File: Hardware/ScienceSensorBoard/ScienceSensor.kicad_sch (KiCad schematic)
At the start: 75 parts, among them U2 OKI-78SR-3.3_1.5-W36H-C

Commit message: Updated BOM and annotation
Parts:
- removed C2: CP1, symbol ScienceSensor-rescue:CP1-Device
- added C2: 10 uF, symbol Device:C_Polarized_US
- gave numbers to parts that had none: 63
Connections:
- net +12V: now also C2.1
- net GND: now also C2.2

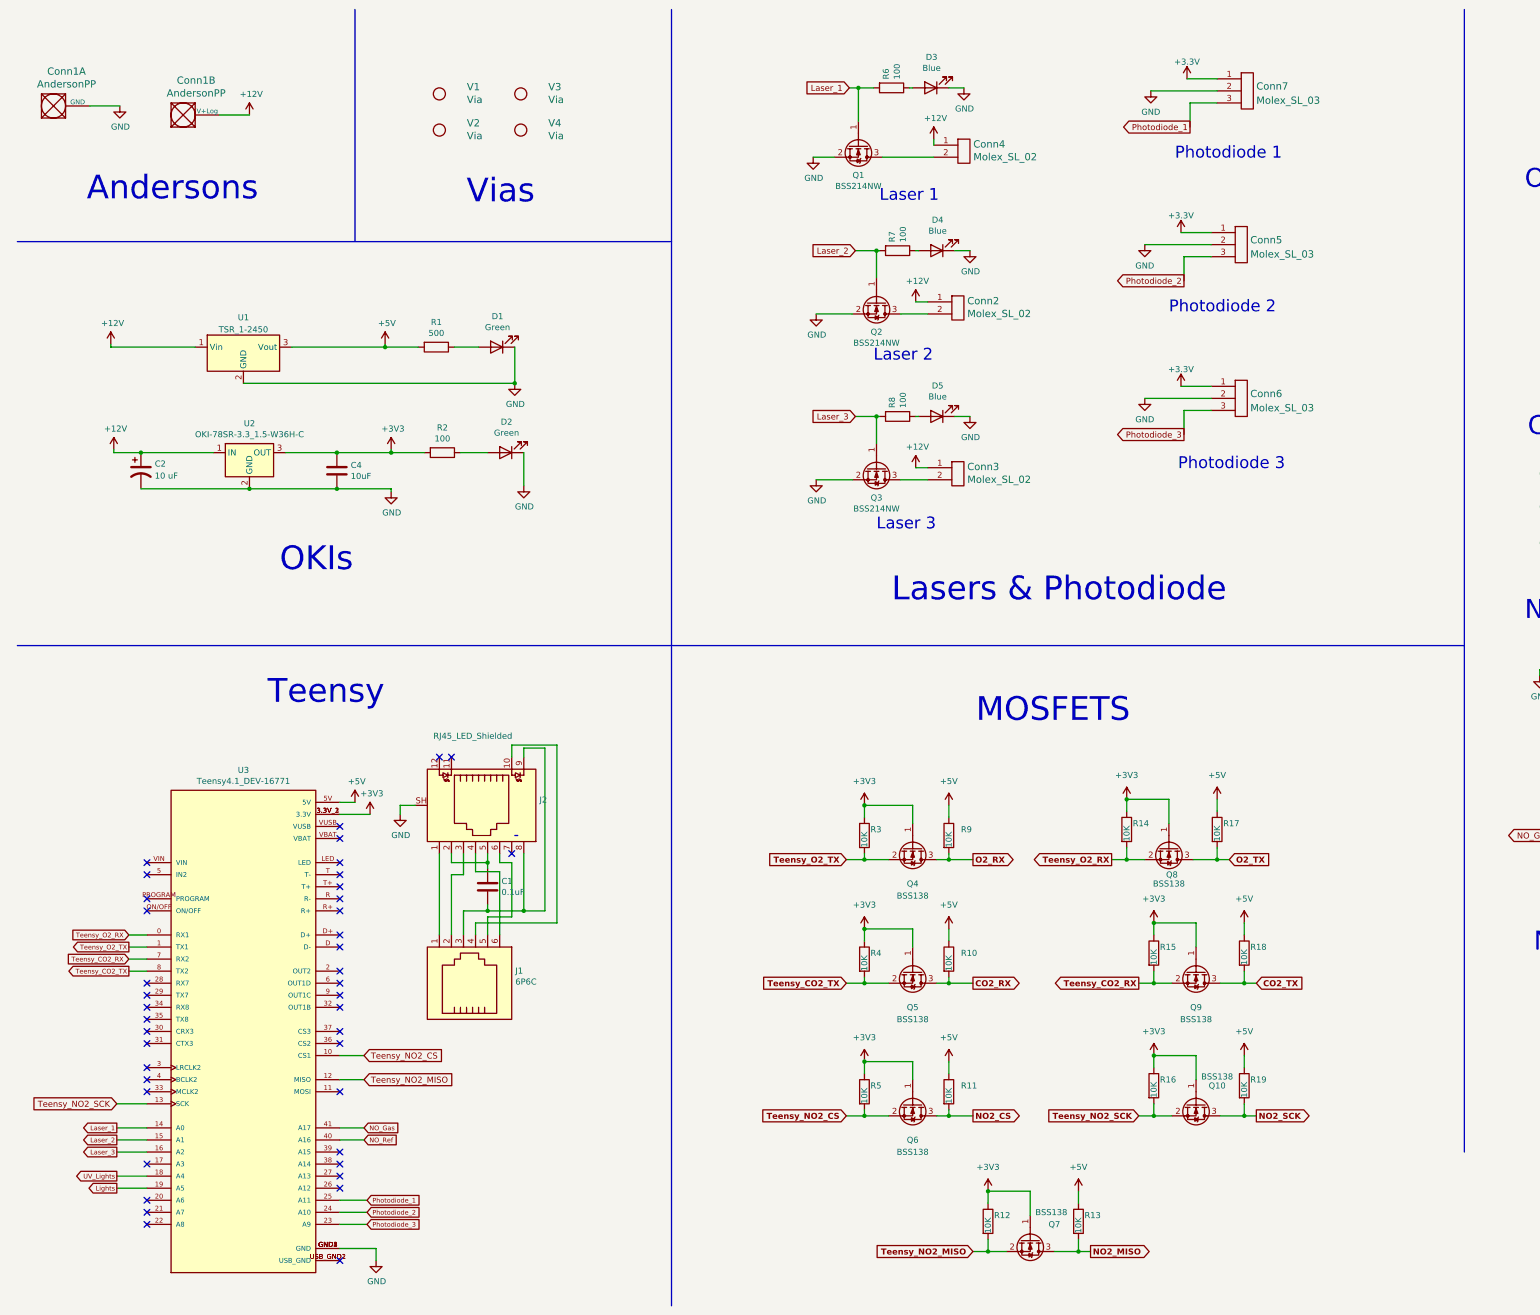
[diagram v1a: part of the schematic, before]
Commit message: Microscope, Fluorometer Breakouts
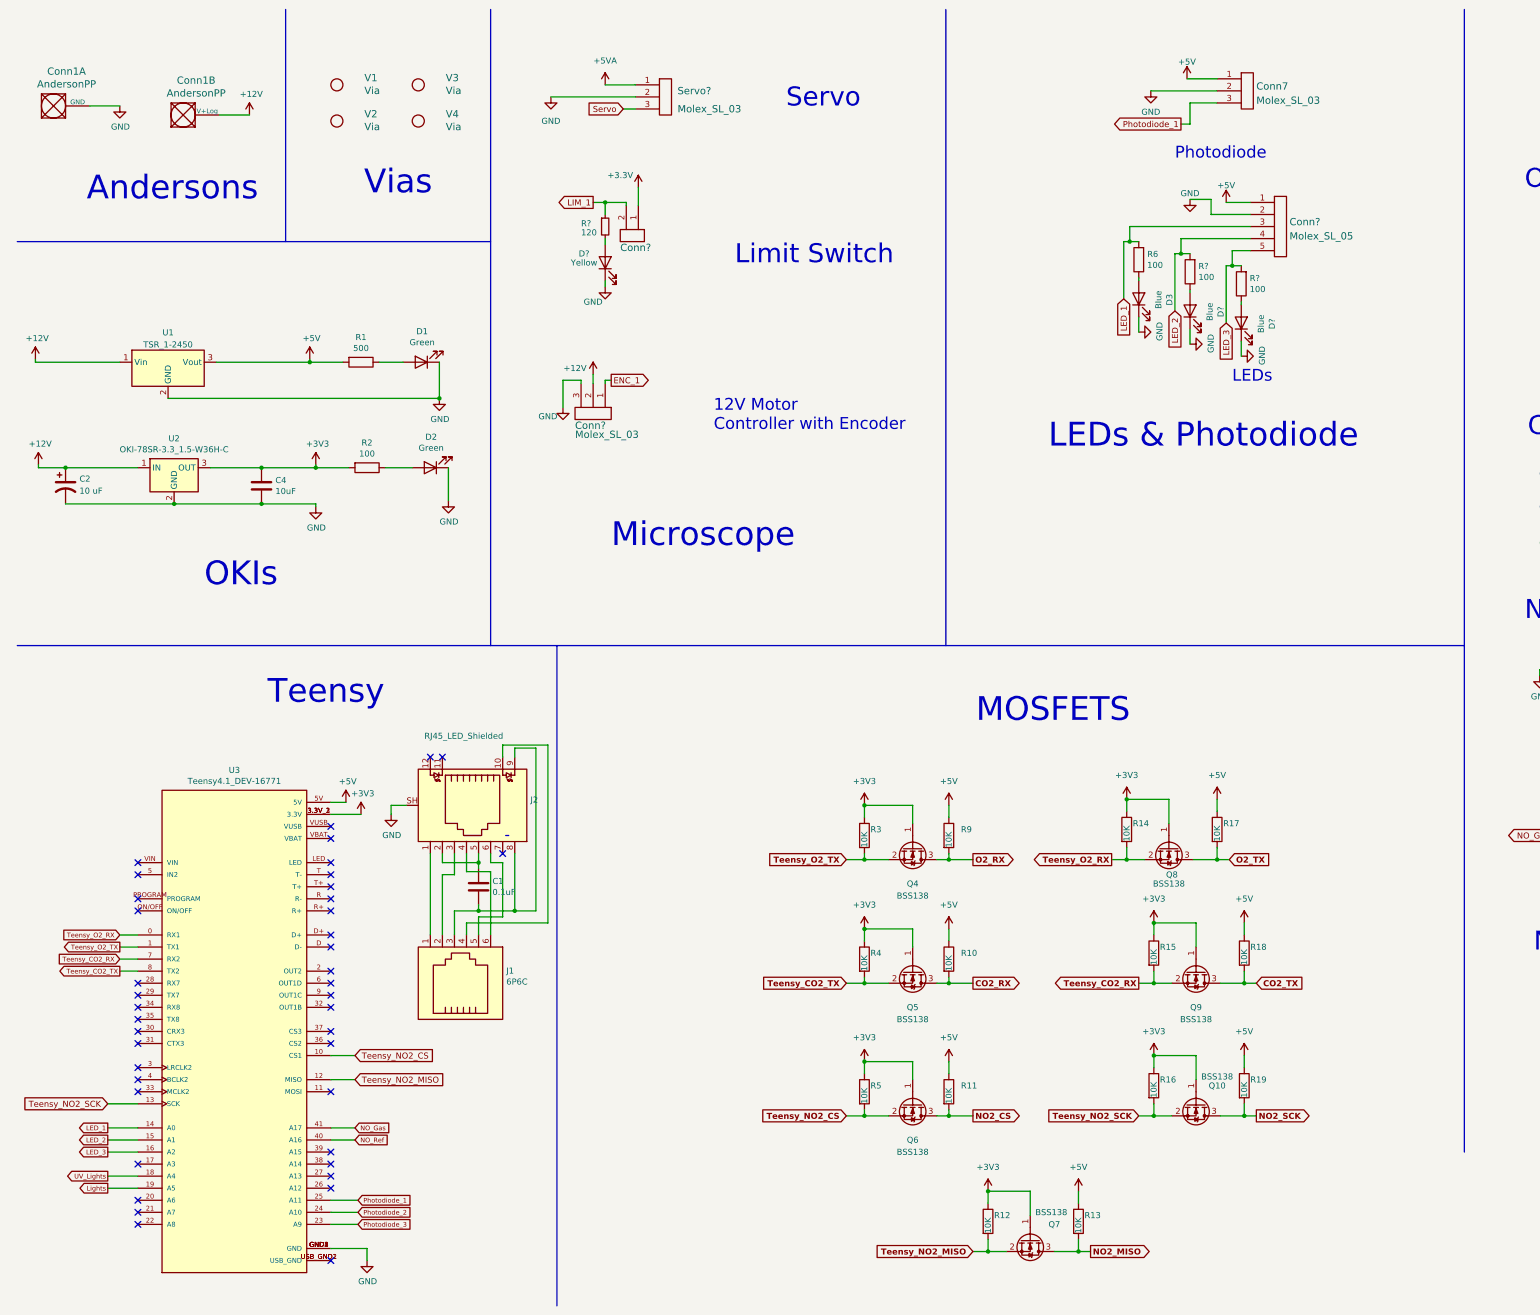
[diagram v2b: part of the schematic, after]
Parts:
- removed Conn2, Conn3, Conn4: Molex_SL_02, symbol MRDT_Connectors:Molex_SL_02
- removed Conn5, Conn6: Molex_SL_03, symbol MRDT_Connectors:Molex_SL_03
- removed D4, D5: Blue, symbol Device:LED
- removed Q1, Q2, Q3: BSS214NW, Package_TO_SOT_SMD:SOT-323_SC-70, symbol Transistor_FET:BSS214NW
- removed R7, R8: 100, symbol Device:R
- added Conn?: Molex_SL_02, MRDT_Connectors:MOLEX_SL_02_Vertical, symbol MRDT_Connectors:Molex_SL_02
- added Conn?: Molex_SL_03, MRDT_Connectors:MOLEX_SL_03_Vertical, symbol MRDT_Connectors:Molex_SL_03
- added Conn?: Molex_SL_05, symbol MRDT_Connectors:Molex_SL_05
- added D? (x2): Blue, symbol Device:LED
- added D?: Yellow, LED_SMD:LED_0603_1608Metric_Pad1.05x0.95mm_HandSolder, symbol Device:LED
- added R?: 120, Resistor_SMD:R_0603_1608Metric_Pad0.98x0.95mm_HandSolder, symbol Device:R_Small
- added R? (x2): 100, symbol Device:R
- added Servo?: Molex_SL_03, symbol MRDT_Connectors:Molex_SL_03
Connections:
- net +3.3V is gone; now on net +5V: Conn7.1
- net +3V3: now also Conn?.1, Conn?.2
- net +5V: now also Conn?.1
- net GND: now also Conn?.2, Conn?.3, D?.1 (K), D?.1 (K), D?.1 (K), Servo?.2
- net Laser_1 renamed LED_1
- net LED_1: now also Conn?.3
- net Laser_2 renamed LED_2
- net LED_2: now also Conn?.4, R?.2
- net Laser_3 renamed LED_3
- net LED_3: now also Conn?.5, R?.2
- new net: D?.2 (A), R?.1 (x2)
- new net: D?.2 (A), R?.2
- new net +5VA: Servo?.1
- new net ENC_1: Conn?.1
- new net LIM_1: Conn?.2, R?.1
- new net Servo: Servo?.3
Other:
- note added: "12V Motor Controller with Encoder"
- note added: "LEDs"
- note added: "LEDs & Photodiode"
- note added: "Limit Switch"
- note added: "Microscope"
- note added: "Photodiode"
- note added: "Servo"
- note removed: "Laser 1"
- note removed: "Laser 2"
- note removed: "Laser 3"
- note removed: "Lasers & Photodiode"
- note removed: "Photodiode 1"
- note removed: "Photodiode 2"
- note removed: "Photodiode 3"
- moved on the sheet: C1, C2, C4, D1, D2, D3, J1, J2, R1, R2, R6, U1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

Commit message: Ethernet
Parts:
- removed J1: 6P6C, symbol Connector:6P6C
- added J1: Conn_02x03_Counter_Clockwise, Connector_PinHeader_2.00mm:PinHeader_2x03_P2.00mm_Vertical, symbol Connector_Generic:Conn_02x03_Counter_Clockwise
- C1: footprint (none) -> Capacitor_SMD:C_0603_1608Metric_Pad1.08x0.95mm_HandSolder
- J2: footprint (none) -> MRDT_Connectors:RJ45_Teensy
- gave numbers to parts that had none: 10
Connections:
- net GND: no longer J2.SH
- net Tx+: now reaches J2.1
- net Tx+: now also J1.1 (Pin_1)
- net at J2.10: now also J1.4 (Pin_4)
- net Tx-: now reaches J2.3
- net Tx-: now also J1.2 (Pin_2)
- net Rx+: now reaches J2.4
- net Rx+: now also J1.6 (Pin_6)
- net Rx-: now reaches J2.6
- net Rx-: now also J1.5 (Pin_5)
- net at C1.2, J2.8, J2.9: now also J1.3 (Pin_3)
- no-connect marks 41 -> 42

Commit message: H-Bridge & Teensy Connections
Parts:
- added C10, C8: 0.1u, Capacitor_SMD:C_0603_1608Metric, symbol Device:C
- added C9: 10u, symbol Device:C_Small
- added Conn5: AndersonPP, MRDT_Connectors:Anderson_2_Horizontal_Side_by_Side, symbol MRDT_Connectors:AndersonPP
- added D11, D14: D_Small, symbol Device:D_Small
- added D12, D13: Pink, symbol Device:LED_Small
- added Q1, Q11, Q2, Q3: SI4156DY, Package_SO:SOIC-8_3.9x4.9mm_P1.27mm, symbol Transistor_FET:FDS2734
- added R29, R30, R33, R34: 100, Resistor_SMD:R_0603_1608Metric_Pad0.98x0.95mm_HandSolder, symbol Device:R
- added R31, R32: 500, Resistor_SMD:R_0603_1608Metric_Pad0.98x0.95mm_HandSolder, symbol Device:R
- added U6, U7: IRS2005S, Package_SO:SOIC-8_3.9x4.9mm_P1.27mm, symbol Driver_FET:IRS2005S
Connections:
- net +5VA is gone; now on net +5V: Servo1.1
- net ENC_1 is gone; now on net Micro_ENC: Conn2.1
- net LIM_1 is gone; now on net Micro_LIM: Conn3.2, R7.1
- net Photodiode_3 is gone; now on net Photodiode_1: U3.23 (A9)
- net Servo is gone; now on net Micro_Servo: Servo1.3
- net +12V: now also D11.2 (A), D14.2 (A), Q1.5 (D), Q1.6 (D), Q1.7 (D), Q1.8 (D), Q3.5 (D), Q3.6 (D), Q3.7 (D), Q3.8 (D), U6.1 (VCC), U7.1 (VCC)
- net GND: now also Q11.1 (S), Q11.2 (S), Q11.3 (S), Q2.1 (S), Q2.2 (S), Q2.3 (S), R31.2, R32.2, U6.4 (COM), U7.4 (COM)
- net Photodiode_1: no longer U3.25 (A11)
- net Micro_Servo: now reaches U3.26 (A12)
- net Micro_ENC: now reaches U3.27 (A13)
- net Micro_LIM: now reaches U3.38 (A14)
- net Lights: no longer names the net of U3.19 (A5)
- net Photodiode_2 renamed Micro_RVS
- net Micro_RVS: now also U6.3 (LIN), U7.2 (HIN)
- net UV_Lights: no longer names the net of U3.18 (A4)
- new net: C8.1, D11.1 (K), U6.8 (VB)
- new net: Q2.4 (G), R30.2
- new net: R30.1, U6.5 (LO)
- new net: Q3.4 (G), R33.2
- new net: R33.1, U7.7 (HO)
- new net: R34.1, U7.5 (LO)
- new net: C10.1, D14.1 (K), U7.8 (VB)
- new net: Q1.4 (G), R29.2
- new net: D12.1 (K), R32.1
- new net: D13.1 (K), R31.1
- new net: R29.1, U6.7 (HO)
- new net: Q11.4 (G), R34.2
- new net M+: C8.2, C9.1, Conn5.1 (GND), D12.2 (A), Q1.1 (S), Q1.2 (S), Q1.3 (S), Q2.5 (D), Q2.6 (D), Q2.7 (D), Q2.8 (D), U6.6 (VS)
- new net M-: C10.2, C9.2, Conn5.2 (V+Log), D13.2 (A), Q11.5 (D), Q11.6 (D), Q11.7 (D), Q11.8 (D), Q3.1 (S), Q3.2 (S), Q3.3 (S), U7.6 (VS)
- new net Micro_FWD: U3.25 (A11), U6.2 (HIN), U7.3 (LIN)
- no-connect marks 42 -> 41
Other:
- note added: "Encoder"
- note added: "H-Bridge"
- note removed: "12V Motor Controller with Encoder"
- moved on the sheet: Conn2, Conn3, Conn4, Conn7, D10, D3, D4, D5, R28, R6, R7, R8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
